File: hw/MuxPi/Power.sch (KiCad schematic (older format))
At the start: 16 parts, among them CON1 PC-GK2.1, Q10 2N7002, Q11 BSO130P03S, U10 LD1117S33CTR

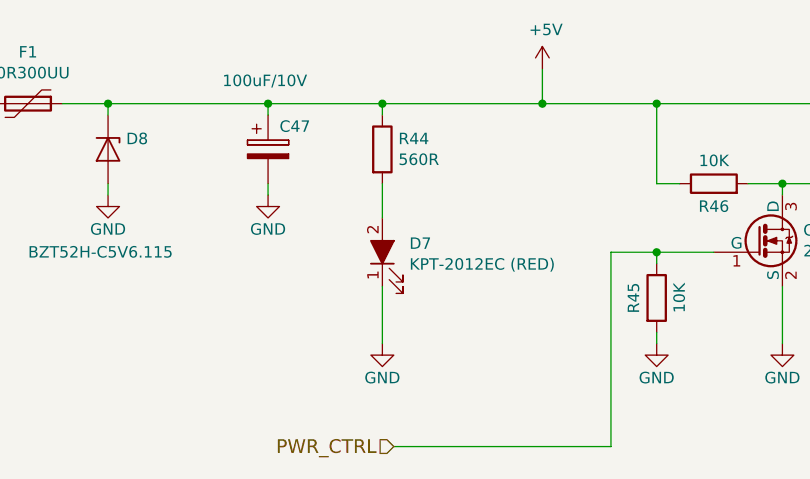
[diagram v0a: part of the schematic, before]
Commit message: Add detailed info to MuxPi electronic components
The additional information includes manufacturer names and
manufacturer symbols for all components except ceramic capacitors
and resistors. It allows to create BOM (Bill Of Materials) with
actual product names.

Change-Id: Id1c518bba60322d4b8b132ad14261806070abc27
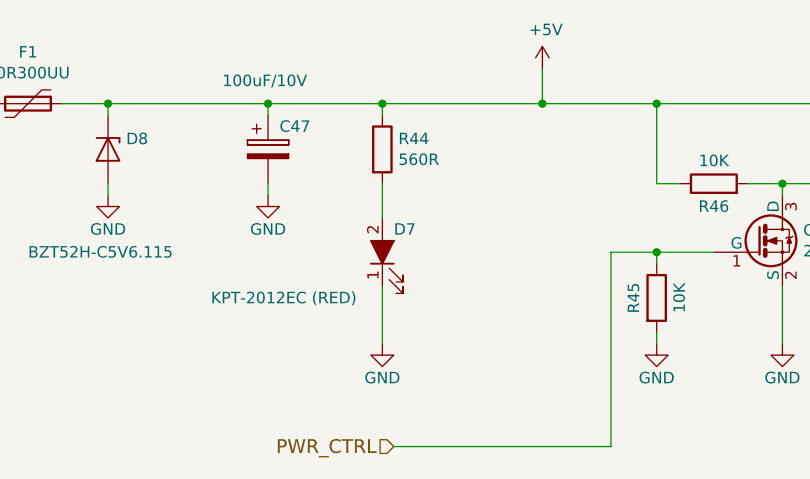
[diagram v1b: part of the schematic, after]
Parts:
- C47: Manufacturer (none) -> KEMET; Symbol (none) -> T491C107K010AT
- C49, C51: Manufacturer (none) -> KEMET; Symbol (none) -> T491A106M016AT
- CON1: Manufacturer (none) -> NINIGI; Symbol (none) -> PC-GK2.1
- D7: Manufacturer (none) -> KINGBRIGHT ELECTRONIC; Symbol (none) -> KPT-2012EC
- D8: Manufacturer (none) -> NEXPERIA; Symbol (none) -> BZT52H-C5V6.115
- F1: Manufacturer (none) -> LITTELFUSE; Symbol (none) -> 30R300UU
- JP3: Manufacturer (none) -> CONNFLY; Shop link (none) -> https://www.tme.eu/pl/details/zl201-02g/listwy-i-gniazda-ko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; Symbol (none) -> DS1021-1*2SF1-1
- Q10: Manufacturer (none) -> ON SEMICONDUCTOR (FAIRCHILD); Symbol (none) -> 2N7002
- Q11: Manufacturer (none) -> INFINEON TECHNOLOGIES; Symbol (none) -> BSO130P03SHXUMA1
- U10: Manufacturer (none) -> ST MICROELECTRONICS; Symbol (none) -> LD1117S33C
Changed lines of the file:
@@
 F 3 "http://www.tme.eu/pl/Document/0ff508dea7a8224c6fb12ae10be076aa/KEM_T2005_T491.pdf" H 7850 3700 50  0001 C CNN
 F 4 "http://www.tme.eu/pl/details/t491a106m016at/kondensatory-tantalowe-smd/kemet/" H 7850 3700 60  0001 C CNN "Shop link"
+F 5 "KEMET" H 7850 3700 50  0001 C CNN "Manufacturer"
+F 6 "T491A106M016AT" H 7850 3700 50  0001 C CNN "Symbol"
 	1    7850 3700
 	1    0    0    -1
@@
 F 3 "http://www.tme.eu/pl/Document/0ff508dea7a8224c6fb12ae10be076aa/KEM_T2005_T491.pdf" H 3550 3700 50  0001 C CNN
 F 4 "http://www.tme.eu/pl/details/t491c107k010at/kondensatory-tantalowe-smd/kemet/" H 3550 3700 60  0001 C CNN "Shop link"
+F 5 "KEMET" H 3550 3700 50  0001 C CNN "Manufacturer"
+F 6 "T491C107K010AT" H 3550 3700 50  0001 C CNN "Symbol"
 	1    3550 3700
 	1    0    0    -1
@@
 F 3 "http://www.tme.eu/pl/Document/0c2caa550314868a0a12e8b9344a6069/pc-gk2.1.pdf" H 1850 3600 50  0001 C CNN
 F 4 "http://www.tme.eu/pl/details/pc-gk2.1/zlacza-dc/ninigi/" H 1850 3600 60  0001 C CNN "Shop link"
+F 5 "NINIGI" H 1850 3600 50  0001 C CNN "Manufacturer"
+F 6 "PC-GK2.1" H 1850 3600 50  0001 C CNN "Symbol"
 	1    1850 3600
 	1    0    0    -1
@@
 F 3 "http://www.tme.eu/pl/Document/bbab3ccbedd9735c8c7032084fb97a45/LD1117.pdf" H 8600 3550 50  0001 C CNN
 F 4 "http://www.tme.eu/pl/details/ld1117s33c/stabilizatory-napiecia-nieregulowane-ldo/st-microelectronics/" H 8600 3550 60  0001 C CNN "Shop link"
+F 5 "ST MICROELECTRONICS" H 8600 3550 50  0001 C CNN "Manufacturer"
+F 6 "LD1117S33C" H 8600 3550 50  0001 C CNN "Symbol"
 	1    8600 3550
 	1    0    0    -1
@@
 Wire Wire Line
 	8600 3800 8600 3900
-$Comp
-L MuxPi:BSO130P03S Q11
-U 1 1 5844A1FE
-P 6750 3700
-F 0 "Q11" H 6750 4207 50  0000 C CNN
-F 1 "BSO130P03S" H 6750 4116 50  0000 C CNN
-F 2 "mux-footprints:SOIC-8" H 6750 4025 50  0001 C CIN
-F 3 "http://www.tme.eu/pl/Document/fde90035d9a6021d44d09086b0d9119c/BSO130P03SHXUMA1-DTE.pdf" V 6750 3700 50  0001 L CNN
-F 4 "http://www.tme.eu/pl/details/bso130p03shxuma1/tranzystory-z-kanalem-p-smd/infineon-technologies/" H 6750 3700 60  0001 C CNN "Shop link"
-	1    6750 3700
-	1    0    0    -1
-$EndComp
 Text HLabel 4100 5000 0    60   Input ~ 0
 PWR_CTRL
@@
 Wire Wire Line
 	5050 5000 4100 5000
-$Comp
-L MuxPi:CP C51
-U 1 1 584AFD5D
-P 9550 3700
-F 0 "C51" H 9600 3800 50  0000 L CNN
-F 1 "10uF/10V" H 9600 3600 50  0000 L CNN
-F 2 "Capacitors_Tantalum_SMD:Tantalum_Case-A_EIA-3216-18_Reflow" H 9588 3550 50  0001 C CNN
-F 3 "http://www.tme.eu/pl/Document/0ff508dea7a8224c6fb12ae10be076aa/KEM_T2005_T491.pdf" H 9550 3700 50  0001 C CNN
-F 4 "http://www.tme.eu/pl/details/t491a106m016at/kondensatory-tantalowe-smd/kemet/" H 9550 3700 60  0001 C CNN "Shop link"
-	1    9550 3700
-	1    0    0    -1
-$EndComp
 $Comp
 L MuxPi:C C50
@@
 $EndComp
 $Comp
-L MuxPi:2N7002 Q10
-U 1 1 584B26D7
-P 5700 4100
-AR Path="/584B26D7" Ref="Q10"  Part="1"
-AR Path="/58449834/584B26D7" Ref="Q10"  Part="1"
-F 0 "Q10" H 5891 4146 50  0000 L CNN
-F 1 "2N7002" H 5891 4055 50  0000 L CNN
-F 2 "TO_SOT_Packages_SMD:SOT-23" H 5900 4025 50  0001 L CIN
-F 3 "https://www.nxp.com/documents/data_sheet/2N7002.pdf" H 5700 4100 50  0001 L CNN
-F 4 "http://www.tme.eu/pl/details/2n7002/tranzystory-z-kanalem-n-smd/fairchild-semiconductor/" H 5700 4100 60  0001 C CNN "Shop link"
-	1    5700 4100
-	1    0    0    -1
-$EndComp
-$Comp
-L MuxPi:LED_ALT D7
-U 1 1 58506DE3
-P 4050 4150
-F 0 "D7" V 4088 4032 50  0000 R CNN
-F 1 "KPT-2012EC (RED)" V 3997 4032 50  0000 R CNN
-F 2 "Diodes_SMD:D_0805" H 4050 4150 50  0001 C CNN
-F 3 "http://www.tme.eu/pl/Document/0a4307e0e1e070f4f6d553134056548e/kpt-2012.pdf" H 4050 4150 50  0001 C CNN
-F 4 "http://www.tme.eu/pl/details/kpt-2012ec/diody-led-smd-kolorowe/kingbright-electronic/" V 4050 4150 60  0001 C CNN "Shop link"
-	1    4050 4150
-	0    -1   -1   0
-$EndComp
-$Comp
 L MuxPi:Polyfuse F1
 U 1 1 58D8D94F
@@
 F 3 "http://www.tme.eu/pl/Document/fdd42053b89d1fd5c6b7e642c2aced3a/Littelfuse_Seria_30R.pdf" H 2500 3500 50  0001 C CNN
 F 4 "http://www.tme.eu/pl/details/30r300uu/bezpieczniki-polimerowe-tht/littelfuse/" H 2500 3500 60  0001 C CNN "Shop link"
+F 5 "LITTELFUSE" V 2500 3500 50  0001 C CNN "Manufacturer"
+F 6 "30R300UU" V 2500 3500 50  0001 C CNN "Symbol"
 	1    2500 3500
 	0    1    1    0
@@
 F 3 "http://www.tme.eu/pl/Document/63e12ac79543603fbb5d1f749bbabbb4/BZT52H-DTE.pdf" H 2850 3700 50  0001 C CNN
 F 4 "http://www.tme.eu/pl/details/bzt52h-c5v6.115/diody-zenera-smd/nexperia/" V 2850 3700 60  0001 C CNN "Shop link"
+F 5 "NEXPERIA" V 2850 3700 50  0001 C CNN "Manufacturer"
+F 6 "BZT52H-C5V6.115" V 2850 3700 50  0001 C CNN "Symbol"
 	1    2850 3700
 	0    1    1    0
@@
 F 1 "Jumper_NO_Small" V 6345 4148 50  0001 L CNN
 F 2 "Pin_Headers:Pin_Header_Straight_1x02_Pitch2.54mm" H 6300 4100 50  0001 C CNN
-F 3 "" H 6300 4100 50  0001 C CNN
+F 3 "https://www.tme.eu/pl/Document/cc301e58a5da78cb543a94b5a5b7f06a/DS1021.pdf" H 6300 4100 50  0001 C CNN
+F 4 "https://www.tme.eu/pl/details/zl201-02g/listwy-i-gniazda-kolkowe/connfly/ds1021-1_2sf1-1/" V 6300 4100 50  0001 C CNN "Shop link"
+F 5 "CONNFLY" V 6300 4100 50  0001 C CNN "Manufacturer"
+F 6 "DS1021-1*2SF1-1" V 6300 4100 50  0001 C CNN "Symbol"
 	1    6300 4100
 	0    1    1    0
@@
 Wire Wire Line
 	6300 3850 6450 3850
+$Comp
+L MuxPi:LED_ALT D7
+U 1 1 5A87E5D9
+P 4050 4150
+F 0 "D7" V 4150 4100 50  0000 R CNN
+F 1 "KPT-2012EC (RED)" V 3850 4900 50  0000 R CNN
+F 2 "Diodes_SMD:D_0805" H 4050 4150 50  0001 C CNN
+F 3 "http://www.tme.eu/pl/Document/0a4307e0e1e070f4f6d553134056548e/kpt-2012.pdf" H 4050 4150 50  0001 C CNN
+F 4 "http://www.tme.eu/pl/details/kpt-2012ec/diody-led-smd-kolorowe/kingbright-electronic/" V 4050 4150 60  0001 C CNN "Shop link"
+F 5 "KINGBRIGHT ELECTRONIC" V 4050 4150 50  0001 C CNN "Manufacturer"
+F 6 "KPT-2012EC" V 4050 4150 50  0001 C CNN "Symbol"
+	1    4050 4150
+	0    -1   -1   0
+$EndComp
+$Comp
+L MuxPi:2N7002 Q10
+U 1 1 5A880A03
+P 5700 4100
+F 0 "Q10" H 5891 4146 50  0000 L CNN
+F 1 "2N7002" H 5891 4055 50  0000 L CNN
+F 2 "TO_SOT_Packages_SMD:SOT-23" H 5900 4025 50  0001 L CIN
+F 3 "https://www.nxp.com/documents/data_sheet/2N7002.pdf" H 5700 4100 50  0001 L CNN
+F 4 "http://www.tme.eu/pl/details/2n7002/tranzystory-z-kanalem-n-smd/fairchild-semiconductor/" H 5700 4100 60  0001 C CNN "Shop link"
+F 5 "ON SEMICONDUCTOR (FAIRCHILD)" H 5700 4100 50  0001 C CNN "Manufacturer"
+F 6 "2N7002" H 5700 4100 50  0001 C CNN "Symbol"
+	1    5700 4100
+	1    0    0    -1
+$EndComp
+$Comp
+L MuxPi:BSO130P03S Q11
+U 1 1 5A881D8D
+P 6750 3700
+F 0 "Q11" H 6750 4207 50  0000 C CNN
+F 1 "BSO130P03S" H 6750 4116 50  0000 C CNN
+F 2 "mux-footprints:SOIC-8" H 6750 4025 50  0001 C CIN
+F 3 "http://www.tme.eu/pl/Document/fde90035d9a6021d44d09086b0d9119c/BSO130P03SHXUMA1-DTE.pdf" V 6750 3700 50  0001 L CNN
+F 4 "http://www.tme.eu/pl/details/bso130p03shxuma1/tranzystory-z-kanalem-p-smd/infineon-technologies/" H 6750 3700 60  0001 C CNN "Shop link"
+F 5 "INFINEON TECHNOLOGIES" H 6750 3700 50  0001 C CNN "Manufacturer"
+F 6 "BSO130P03SHXUMA1" H 6750 3700 50  0001 C CNN "Symbol"
+	1    6750 3700
+	1    0    0    -1
+$EndComp
+$Comp
+L MuxPi:CP C51
+U 1 1 5A884D9F
+P 9550 3700
+F 0 "C51" H 9600 3800 50  0000 L CNN
+F 1 "10uF/10V" H 9600 3600 50  0000 L CNN
+F 2 "Capacitors_Tantalum_SMD:Tantalum_Case-A_EIA-3216-18_Reflow" H 9588 3550 50  0001 C CNN
+F 3 "http://www.tme.eu/pl/Document/0ff508dea7a8224c6fb12ae10be076aa/KEM_T2005_T491.pdf" H 9550 3700 50  0001 C CNN
+F 4 "http://www.tme.eu/pl/details/t491a106m016at/kondensatory-tantalowe-smd/kemet/" H 9550 3700 60  0001 C CNN "Shop link"
+F 5 "KEMET" H 9550 3700 50  0001 C CNN "Manufacturer"
+F 6 "T491A106M016AT" H 9550 3700 50  0001 C CNN "Symbol"
+	1    9550 3700
+	1    0    0    -1
+$EndComp
 $EndSCHEMATC

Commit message: Update  hardware design to version 1.4
Change-Id: I72a4381d8bec5616bc1cfe04dc8a5407141c77d5
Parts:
- F1: value 30R300UU -> 0ZCG0300FF2B; footprint Fuse_Holders_and_Fuses:Fuse_TE5_Littlefuse-395Series -> MuxPi:Fuse_1812_4532Metric; Manufacturer LITTELFUSE -> BEL FUSE; Shop link http://www.tme.eu/pl/details/30r300uu/bezpieczniki-polimero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 -> https://pl.mouser.com/ProductDetail/Bel-Fuse/0ZCG0300FF2B?q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; Symbol 30R300UU -> 0ZCG0300FF2B
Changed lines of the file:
@@
 EESchema Schematic File Version 4
 LIBS:MuxPi-cache
-EELAYER 26 0
+EELAYER 29 0
 EELAYER END
 $Descr A4 11693 8268
@@
 Sheet 10 12
 Title "MuxPi"
-Date "2018-08-14"
-Rev "1.3"
+Date "2018-11-16"
+Rev "1.4"
 Comp "SRPOL"
 Comment1 "Author: Adam Malinowski <a.malinowsk2@partner.samsung.com>"
@@
 P 2500 3500
 F 0 "F1" V 2275 3500 50  0000 C CNN
-F 1 "30R300UU" V 2366 3500 50  0000 C CNN
-F 2 "Fuse_Holders_and_Fuses:Fuse_TE5_Littlefuse-395Series" H 2550 3300 50  0001 L CNN
-F 3 "http://www.tme.eu/pl/Document/fdd42053b89d1fd5c6b7e642c2aced3a/Littelfuse_Seria_30R.pdf" H 2500 3500 50  0001 C CNN
-F 4 "http://www.tme.eu/pl/details/30r300uu/bezpieczniki-polimerowe-tht/littelfuse/" H 2500 3500 60  0001 C CNN "Shop link"
-F 5 "LITTELFUSE" V 2500 3500 50  0001 C CNN "Manufacturer"
-F 6 "30R300UU" V 2500 3500 50  0001 C CNN "Symbol"
+F 1 "0ZCG0300FF2B" V 2366 3500 50  0000 C CNN
+F 2 "MuxPi:Fuse_1812_4532Metric" H 2550 3300 50  0001 L CNN
+F 3 "https://pl.mouser.com/datasheet/2/643/0ZCG_Nov2016-1132141.pdf" H 2500 3500 50  0001 C CNN
+F 4 "https://pl.mouser.com/ProductDetail/Bel-Fuse/0ZCG0300FF2B?qs=sGAEpiMZZMsgjL4JkW1EEcd%252bb5fzYQwTOL%252bTuYbNnH2xaTnv9I3X0Q%3d%3d" H 2500 3500 60  0001 C CNN "Shop link"
+F 5 "BEL FUSE" V 2500 3500 50  0001 C CNN "Manufacturer"
+F 6 "0ZCG0300FF2B" V 2500 3500 50  0001 C CNN "Symbol"
 	1    2500 3500
 	0    1    1    0
